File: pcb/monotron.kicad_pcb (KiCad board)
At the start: 2 copper layers, 134.1 x 94 mm, 57 parts, among them J1 Mono / Stereo, J10 DIN5-180, J11 DIN5-180, J12 DE9M, J13 DB25_Female, J14 Mini-DIN-6, J15 Mini-DIN-6, J2 Jack-DC, J3 1x7 Header, J4 AudioJack3, J5 DE9F, J6 1x4 Header, J7 DE15HD, J8 2x6 Header, J9 DIN5-180, U1 TM4C123G_Launchpad, U2 MAX3232, U3 74LS14, U4 6N138, U5 ATmega48A-PU, U6 MCP7940N-xP, Y1 32,768 kHz

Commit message: WIP re-laying out board.
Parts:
- added D2: 1N4148, Diode_THT:D_DO-35_SOD27_P7.62mm_Horizontal, F.Cu at (128.3, 74.9)
- added H1: DP14085, Monotron:DP14085, F.Cu at (67.3, 44.5)
- added J16: Micro_SD_Card_Det, Connector_Card:microSD_HC_Hirose_DM3D-SF, F.Cu at (163.4, 52.3)
- added J17: DNF, Connector_PinHeader_2.54mm:PinHeader_1x07_P2.54mm_Vertical, F.Cu at (176.5, 64.8)
- added R17: 330, Resistor_THT:R_Axial_DIN0204_L3.6mm_D1.6mm_P5.08mm_Horizontal, F.Cu at (239.5, 57.0)
- added R18: 47k, Resistor_THT:R_Axial_DIN0204_L3.6mm_D1.6mm_P5.08mm_Horizontal, F.Cu at (244.5, 50.3)
- added R19: 47k, Resistor_THT:R_Axial_DIN0204_L3.6mm_D1.6mm_P5.08mm_Horizontal, F.Cu at (247.9, 43.6)
- added R20: 47k, Resistor_THT:R_Axial_DIN0204_L3.6mm_D1.6mm_P5.08mm_Horizontal, F.Cu at (240.3, 52.5)
- added R21: 47k, Resistor_THT:R_Axial_DIN0204_L3.6mm_D1.6mm_P5.08mm_Horizontal, F.Cu at (234.5, 61.4)
- C1: value 10u -> 100n; footprint Capacitor_THT:C_Radial_D5.0mm_H5.0mm_P2.00mm -> Capacitor_THT:C_Disc_D5.0mm_W2.5mm_P2.50mm
- C10, C9: value 470n -> 33n
- C11, C12, C13: value 100n -> 470n
- C15, C16: value 12p -> 10u; footprint Capacitor_THT:C_Disc_D4.7mm_W2.5mm_P5.00mm -> Capacitor_THT:C_Radial_D5.0mm_H5.0mm_P2.00mm
- C2: value 10u -> 47u
- C3: value 47u -> 100n; footprint Capacitor_THT:C_Radial_D5.0mm_H5.0mm_P2.00mm -> Capacitor_THT:C_Disc_D5.0mm_W2.5mm_P2.50mm
- C4, C5: value 33n -> 12p
- C8: value 470n -> 100n
- D1: value 1N4148 -> LED; footprint Diode_THT:D_A-405_P12.70mm_Horizontal -> LED_THT:LED_D3.0mm
- J1: value Mono / Stereo -> 2.1mm DC Jack; footprint Connector_PinHeader_2.54mm:PinHeader_1x03_P2.54mm_Vertical -> Connector_BarrelJack:BarrelJack_CUI_PJ-102AH_Horizontal
- J10: value DIN5-180 -> 1x3 Header; footprint Monotron:5P180 DIN Socket -> Connector_PinHeader_2.54mm:PinHeader_1x03_P2.54mm_Vertical
- J11: value DIN5-180 -> DE9M; footprint Monotron:5P180 DIN Socket -> Connector_Dsub:DSUB-9_Male_Horizontal_P2.77x2.84mm_EdgePinOffset7.70mm_Housed_MountingHolesOffset9.12mm
- J12: value DE9M -> Mini-DIN-6; footprint Connector_Dsub:DSUB-9_Male_Horizontal_P2.77x2.84mm_EdgePinOffset7.70mm_Housed_MountingHolesOffset9.12mm -> Monotron:mini-DIN 6
- J13: value DB25_Female -> Mini-DIN-6; footprint Connector_Dsub:DSUB-25_Male_Horizontal_P2.77x2.84mm_EdgePinOffset7.70mm_Housed_MountingHolesOffset9.12mm -> Monotron:mini-DIN 6
- J14: value Mini-DIN-6 -> DB25_Female; footprint Monotron:mini-DIN 6 -> Connector_Dsub:DSUB-25_Male_Horizontal_P2.77x2.84mm_EdgePinOffset7.70mm_Housed_MountingHolesOffset9.12mm
- J15: value Mini-DIN-6 -> DE15HD; footprint Monotron:mini-DIN 6 -> Connector_Dsub:DSUB-15-HD_Female_Horizontal_P2.29x1.98mm_EdgePinOffset8.35mm_Housed_MountingHolesOffset10.89mm
- J2: value Jack-DC -> DE9M; footprint Connector_BarrelJack:BarrelJack_CUI_PJ-102AH_Horizontal -> Connector_Dsub:DSUB-9_Male_Horizontal_P2.77x2.84mm_EdgePinOffset7.70mm_Housed_MountingHolesOffset9.12mm
- J3: value 1x7 Header -> 1x4 Header; footprint Connector_PinHeader_2.54mm:PinHeader_1x07_P2.54mm_Vertical -> Connector_PinHeader_2.54mm:PinHeader_1x04_P2.54mm_Vertical
- J4: value AudioJack3 -> DIN5-180; footprint Connector_Audio:Jack_3.5mm_CUI_SJ1-3533NG_Horizontal -> Monotron:5P180 DIN Socket
- J5: value DE9F -> DIN5-180; footprint Connector_Dsub:DSUB-9_Male_Horizontal_P2.77x2.84mm_EdgePinOffset7.70mm_Housed_MountingHolesOffset9.12mm -> Monotron:5P180 DIN Socket
- J6: value 1x4 Header -> DIN5-180; footprint Connector_PinHeader_2.54mm:PinHeader_1x04_P2.54mm_Vertical -> Monotron:5P180 DIN Socket
- J7: value DE15HD -> 2x6 Header; footprint Connector_Dsub:DSUB-15-HD_Female_Horizontal_P2.29x1.98mm_EdgePinOffset8.35mm_Housed_MountingHolesOffset10.89mm -> Connector_PinHeader_2.54mm:PinHeader_2x06_P2.54mm_Vertical
- J8: value 2x6 Header -> 2x3 Header; footprint Connector_PinHeader_2.54mm:PinHeader_2x06_P2.54mm_Vertical -> Connector_PinHeader_2.54mm:PinHeader_2x03_P2.54mm_Vertical
- J9: value DIN5-180 -> 3.5mm TRS Jack; footprint Monotron:5P180 DIN Socket -> Connector_Audio:Jack_3.5mm_CUI_SJ1-3533NG_Horizontal
- R1: value 150 -> 470; footprint Resistor_THT:R_Axial_DIN0207_L6.3mm_D2.5mm_P2.54mm_Vertical -> Resistor_THT:R_Axial_DIN0204_L3.6mm_D1.6mm_P5.08mm_Horizontal
- R10: footprint Resistor_THT:R_Axial_DIN0411_L9.9mm_D3.6mm_P5.08mm_Vertical -> Resistor_THT:R_Axial_DIN0204_L3.6mm_D1.6mm_P5.08mm_Horizontal
- R11, R12: value 220 -> 270; footprint Resistor_THT:R_Axial_DIN0411_L9.9mm_D3.6mm_P5.08mm_Vertical -> Resistor_THT:R_Axial_DIN0204_L3.6mm_D1.6mm_P5.08mm_Horizontal
- R13, R14: value 220 -> 150; footprint Resistor_THT:R_Axial_DIN0411_L9.9mm_D3.6mm_P5.08mm_Vertical -> Resistor_THT:R_Axial_DIN0204_L3.6mm_D1.6mm_P5.08mm_Horizontal
- R15: value 10K -> 330; footprint Resistor_THT:R_Axial_DIN0411_L9.9mm_D3.6mm_P5.08mm_Vertical -> Resistor_THT:R_Axial_DIN0204_L3.6mm_D1.6mm_P5.08mm_Horizontal
- R16: value 470 -> 330; footprint Resistor_THT:R_Axial_DIN0411_L9.9mm_D3.6mm_P12.70mm_Horizontal -> Resistor_THT:R_Axial_DIN0204_L3.6mm_D1.6mm_P5.08mm_Horizontal
- R2: value 150 -> 10K; footprint Resistor_THT:R_Axial_DIN0207_L6.3mm_D2.5mm_P2.54mm_Vertical -> Resistor_THT:R_Axial_DIN0204_L3.6mm_D1.6mm_P5.08mm_Horizontal
- R3: value 270 -> 470; footprint Resistor_THT:R_Axial_DIN0207_L6.3mm_D2.5mm_P2.54mm_Vertical -> Resistor_THT:R_Axial_DIN0204_L3.6mm_D1.6mm_P5.08mm_Horizontal
- R4: value 270 -> 4.7k; footprint Resistor_THT:R_Axial_DIN0207_L6.3mm_D2.5mm_P2.54mm_Vertical -> Resistor_THT:R_Axial_DIN0204_L3.6mm_D1.6mm_P5.08mm_Horizontal
- R5: footprint Resistor_THT:R_Axial_DIN0411_L9.9mm_D3.6mm_P12.70mm_Horizontal -> Resistor_THT:R_Axial_DIN0204_L3.6mm_D1.6mm_P5.08mm_Horizontal
- R6: value 4.7k -> 220; footprint Resistor_THT:R_Axial_DIN0411_L9.9mm_D3.6mm_P12.70mm_Horizontal -> Resistor_THT:R_Axial_DIN0204_L3.6mm_D1.6mm_P5.08mm_Horizontal
- R7, R8, R9: value 330 -> 220; footprint Resistor_THT:R_Axial_DIN0411_L9.9mm_D3.6mm_P12.70mm_Horizontal -> Resistor_THT:R_Axial_DIN0204_L3.6mm_D1.6mm_P5.08mm_Horizontal
- U1: value TM4C123G_Launchpad -> 74LS14; footprint Launchpad:Launchpad_4x10 -> Package_DIP:DIP-14_W7.62mm
- U2: value MAX3232 -> 6N138; footprint Package_DIP:DIP-16_W7.62mm -> Package_DIP:DIP-8_W7.62mm
- U3: value 74LS14 -> MCP7940N-xP; footprint Package_DIP:DIP-14_W7.62mm -> Package_DIP:DIP-8_W7.62mm
- U4: value 6N138 -> TM4C123G_Launchpad; footprint Package_DIP:DIP-8_W7.62mm -> Monotron:Launchpad_4x10
- U6: value MCP7940N-xP -> MAX3232; footprint Package_DIP:DIP-8_W7.62mm -> Package_DIP:DIP-16_W7.62mm
- moved C3 159.9 mm to (229.5, 109.4), turned to 90 degrees
- moved J12 133.2 mm to (67.7, 80.0), turned to 90 degrees
- moved R16 128.6 mm to (243.7, 34.4)
- moved R6 126.9 mm to (237.9, 36.6)
- moved J11 121.8 mm to (77.8, 98.7), turned to 270 degrees
- moved J3 118.1 mm to (194.3, 82.5)
- moved R8 117.9 mm to (216.9, 45.5)
- moved R7 117.7 mm to (212.4, 51.4)
- moved R9 115.3 mm to (218.6, 43.3)
- moved J2 99.9 mm to (151.1, 120.7), turned to 0 degrees
- moved J13 98.1 mm to (67.7, 61.4), turned to 90 degrees
- moved C11 90.3 mm to (92.8, 102.9), turned to 0 degrees
- moved BT1 84.3 mm to (110.5, 77.5), turned to 180 degrees
- moved C17 82.2 mm to (238.7, 124.7)
- moved C14 79.6 mm to (231.1, 71.3), turned to 270 degrees
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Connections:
- net /DSR renamed Net-(J12-Pad6)
- C1 pad 1: Net-(C1-Pad1) -> +5V
- C1 pad 2: Net-(C1-Pad2) -> GND
- C10 pad 1: GND -> Net-(C10-Pad1)
- C10 pad 2: Net-(C10-Pad2) -> GND
- C11 pad 1: +5V -> Net-(C11-Pad1)
- C11 pad 2: GND -> Net-(C11-Pad2)
- C12 pad 1: +5V -> Net-(C12-Pad1)
- C12 pad 2: GND -> Net-(C12-Pad2)
- C13 pad 1: +5V -> GND
- C13 pad 2: GND -> Net-(C13-Pad2)
- C15 pad 1: GND -> Net-(C15-Pad1)
- C16 pad 1: GND -> Net-(C10-Pad1)
- C17 pad 1: +3V3 -> Net-(C12-Pad1)
- C2 pad 1: Net-(C2-Pad1) -> +5V
- C2 pad 2: Net-(C2-Pad2) -> GND
- C3 pad 1: +5V -> +3V3
- C4 pad 1: Net-(C1-Pad1) -> GND
- C4 pad 2: GND -> Net-(C4-Pad2)
- C5 pad 1: Net-(C2-Pad1) -> GND
- C5 pad 2: GND -> Net-(C5-Pad2)
- C7 pad 1: Net-(C7-Pad1) -> +5V
- C8 pad 1: Net-(C8-Pad1) -> +5V
- C8 pad 2: Net-(C8-Pad2) -> GND
- C9 pad 1: Net-(C7-Pad1) -> Net-(C15-Pad1)
- C9 pad 2: Net-(C9-Pad2) -> GND
- D1 pad 1: Net-(D1-Pad1) -> /PD2_SD_ACT
- J1 pad 1: Net-(C1-Pad2) -> +5V
- J1 pad 2: Net-(J1-Pad2) -> GND
- J1 pad 3: Net-(C2-Pad2) -> (no net)
- J10 pad 1: Net-(J10-Pad1) -> Net-(C15-Pad2)
- J10 pad 2: GND -> Net-(J10-Pad2)
- J10 pad 3: Net-(J10-Pad3) -> Net-(C16-Pad2)
- J11 pad 2: Net-(J11-Pad2) -> /RS232_RX
- J11 pad 3: Net-(J11-Pad3) -> /RS232_TX
- J11 pad 5: Net-(D1-Pad2) -> GND
- J11 pad 6: (no net) -> Net-(J11-Pad6)
- J11 pad 7: (no net) -> /RS232_RTS
- J12 pad 1: /DCD -> /KB_DATA
- J12 pad 2: /RS232_RX -> Net-(J12-Pad2)
- J12 pad 3: /RS232_TX -> GND
- J12 pad 4: /DTR -> +5V
- J12 pad 5: GND -> /KB_CLK
- J12 pad 7: /RS232_RTS -> (no net)
- J12 pad 8: /RS232_CTS -> (no net)
- J12 pad 9: /RI -> (no net)
- J13 pad 1: /Monotron I/O Expansion/STROBE -> /MS_DATA
- J13 pad 2: /Monotron I/O Expansion/D0 -> Net-(J13-Pad2)
- J13 pad 3: /Monotron I/O Expansion/D1 -> GND
- J13 pad 4: /Monotron I/O Expansion/D2 -> +5V
- J13 pad 5: /Monotron I/O Expansion/D3 -> /MS_CLK
- J13 pad 6: /Monotron I/O Expansion/D4 -> Net-(J13-Pad6)
- J13 pad 7: /Monotron I/O Expansion/D5 -> (no net)
- J13 pad 8: /Monotron I/O Expansion/D6 -> (no net)
- J13 pad 9: /Monotron I/O Expansion/D7 -> (no net)
- J14 pad 1: /Monotron I/O Expansion/KB_DATA -> /STROBE
- J14 pad 2: Net-(J14-Pad2) -> /D0
- J14 pad 3: GND -> /D1
- J14 pad 4: +5V -> /D2
- J14 pad 5: /Monotron I/O Expansion/KB_CLK -> /D3_MOSI
- J14 pad 6: Net-(J14-Pad6) -> /D4_MISO
- J14 pad 7: (no net) -> /D5_SCK
- J14 pad 8: (no net) -> /D6
- J14 pad 9: (no net) -> /D7
- J15 pad 1: /Monotron I/O Expansion/MS_DATA -> Net-(J15-Pad1)
- J15 pad 3: GND -> Net-(J15-Pad3)
- J15 pad 4: +5V -> Net-(J15-Pad4)
- J15 pad 5: /Monotron I/O Expansion/MS_CLK -> GND
- J15 pad 6: Net-(J15-Pad6) -> GND
- J15 pad 7: (no net) -> GND
- J15 pad 8: (no net) -> GND
- J15 pad 9: (no net) -> Net-(J15-Pad9)
- J2 pad 1: +5V -> /PE2_JS_UP
- J2 pad 2: GND -> /PE3_JS_DOWN
- J2 pad 3: (no net) -> /PD6_JS_LEFT
- J3 pad 1: Net-(J3-Pad1) -> GND
- J3 pad 2: /PA4_SD_MISO -> +5V
- J3 pad 3: GND -> /PA7_I2C_SDA
- J3 pad 4: /PA2_SD_CLK -> /PA6_I2C_SCL
- J5 pad 1: /PE2_JS_UP -> Net-(J5-Pad1)
- J5 pad 2: /PE3_JS_DOWN -> Net-(J5-Pad2)
- J5 pad 3: /PD6_JS_LEFT -> Net-(J5-Pad3)
- J5 pad 4: /PD7_JS_RIGHT -> Net-(J5-Pad4)
- J5 pad 5: Net-(J5-Pad5) -> Net-(D2-Pad1)
- J5 pad 6: /PF4_JS_FIRE -> (no net)
- J5 pad 7: Net-(J5-Pad7) -> (no net)
- J6 pad 1: GND -> Net-(J6-Pad1)
- J6 pad 2: +5V -> GND
- J6 pad 3: /PA7_I2C_SDA -> Net-(J6-Pad3)
- J6 pad 4: /PA6_I2C_SCL -> Net-(J6-Pad4)
- J7 pad 1: Net-(J7-Pad1) -> GND
- J7 pad 10: Net-(J7-Pad10) -> /PB0_U1RX
- J7 pad 11: Net-(J7-Pad11) -> Net-(C12-Pad1)
- J7 pad 12: Net-(J7-Pad12) -> +3V3
- J7 pad 2: Net-(J7-Pad2) -> GND
- J7 pad 4: Net-(J7-Pad4) -> /PC5_U1CTS
- J7 pad 5: GND -> Net-(J7-Pad5)
- J7 pad 6: GND -> /PC4_U1RTS
- J7 pad 7: GND -> Net-(J7-Pad7)
- J7 pad 8: GND -> /PB1_U1TX
- J8 pad 1: GND -> /D4_MISO
- J8 pad 2: GND -> +5V
- J8 pad 3: /DTE_CTS -> /D5_SCK
- J8 pad 4: /PC5_U1CTS -> /D3_MOSI
- J8 pad 5: /DTE_RTS -> Net-(J8-Pad5)
- J8 pad 6: /PC4_U1RTS -> GND
- R1 pad 1: Net-(C1-Pad1) -> +3V3
- R1 pad 2: GND -> /PC6_MIDI_IN
- R10 pad 2: Net-(J9-Pad4) -> Net-(J6-Pad4)
- R11 pad 1: +5V -> /PE4_AUDIO_L
- R11 pad 2: Net-(J10-Pad4) -> Net-(C15-Pad1)
- R12 pad 1: Net-(R12-Pad1) -> /PE5_AUDIO_R
- R12 pad 2: Net-(J10-Pad5) -> Net-(C10-Pad1)
- R13 pad 1: Net-(J9-Pad5) -> Net-(C15-Pad1)
- R13 pad 2: Net-(R13-Pad2) -> GND
- R14 pad 1: Net-(D1-Pad1) -> Net-(C10-Pad1)
- R14 pad 2: Net-(J11-Pad4) -> GND
- R15 pad 1: Net-(R15-Pad1) -> Net-(J15-Pad1)
- R15 pad 2: GND -> /PF1_VGA_RED
- R16 pad 1: +3V3 -> Net-(J15-Pad2)
- R16 pad 2: /PC6_MIDI_IN -> /PB7_VGA_GRN
- R2 pad 1: Net-(C2-Pad1) -> Net-(R2-Pad1)
- R3 pad 1: /PE4_AUDIO_L -> Net-(D1-Pad2)
- R3 pad 2: Net-(C1-Pad1) -> +3V3
- R4 pad 1: /PE5_AUDIO_R -> /PA6_I2C_SCL
- R4 pad 2: Net-(C2-Pad1) -> +5V
- R5 pad 1: /PA6_I2C_SCL -> +5V
- R5 pad 2: +5V -> /PA7_I2C_SDA
- R6 pad 1: +5V -> Net-(R6-Pad1)
- R6 pad 2: /PA7_I2C_SDA -> Net-(J4-Pad5)
- R7 pad 1: Net-(J7-Pad1) -> Net-(R7-Pad1)
- R7 pad 2: /PF1_VGA_RED -> Net-(J6-Pad5)
- R8 pad 1: Net-(J7-Pad2) -> Net-(D2-Pad2)
- R8 pad 2: /PB7_VGA_GRN -> Net-(J5-Pad4)
- R9 pad 1: Net-(J7-Pad3) -> +5V
- R9 pad 2: /PD3_VGA_BLU -> Net-(J4-Pad4)
- U2 pad 1: Net-(C6-Pad1) -> Net-(U2-Pad1)
- U2 pad 2: Net-(C9-Pad2) -> Net-(D2-Pad1)
- U2 pad 3: Net-(C6-Pad2) -> Net-(D2-Pad2)
- U2 pad 4: Net-(C8-Pad1) -> Net-(U2-Pad4)
- U2 pad 5: Net-(C8-Pad2) -> GND
- U2 pad 6: Net-(C10-Pad2) -> /PC6_MIDI_IN
- U2 pad 7: /RS232_RTS -> Net-(R2-Pad1)
- U2 pad 8: /RS232_CTS -> +5V
- U3 pad 1: /PC6_MIDI_IN -> Net-(C4-Pad2)
- U3 pad 2: Net-(U3-Pad2) -> Net-(C5-Pad2)
- U3 pad 3: Net-(U3-Pad3) -> +BATT
- U3 pad 4: Net-(R13-Pad2) -> GND
- U3 pad 5: Net-(U3-Pad2) -> /PA7_I2C_SDA
- U3 pad 6: Net-(R12-Pad1) -> /PA7_I2C_SDA
- U3 pad 7: GND -> Net-(U3-Pad7)
- U3 pad 8: Net-(U3-Pad3) -> +3V3
- U5 pad 1: /Monotron I/O Expansion/SELPRIN -> Net-(J8-Pad5)
- U5 pad 10: /Monotron I/O Expansion/D7 -> /D7
- U5 pad 11: /Monotron I/O Expansion/ERROR -> /ERROR
- U5 pad 12: /Monotron I/O Expansion/AUTOF -> /AUTOF
- U5 pad 13: /Monotron I/O Expansion/STROBE -> /STROBE
- U5 pad 14: /Monotron I/O Expansion/D0 -> /D0
- U5 pad 15: /Monotron I/O Expansion/D1 -> /D1
- U5 pad 16: /Monotron I/O Expansion/D2 -> /D2
- U5 pad 17: /Monotron I/O Expansion/D3 -> /D3_MOSI
- U5 pad 18: /Monotron I/O Expansion/D4 -> /D4_MISO
- U5 pad 19: /Monotron I/O Expansion/D5 -> /D5_SCK
- U5 pad 2: /PE1_U7TX -> /PE0_U7RX
- U5 pad 23: /Monotron I/O Expansion/KB_CLK -> /KB_CLK
- U5 pad 24: /Monotron I/O Expansion/MS_CLK -> /MS_CLK
- U5 pad 25: /Monotron I/O Expansion/KB_DATA -> /KB_DATA
- U5 pad 26: /Monotron I/O Expansion/MS_DATA -> /MS_DATA
- U5 pad 27: /Monotron I/O Expansion/INIT -> /SELPRIN
- U5 pad 28: /Monotron I/O Expansion/SEL -> /SEL
- U5 pad 3: /PE0_U7RX -> /PE1_U7TX
- U5 pad 4: /Monotron I/O Expansion/ACK -> /ACK
- U5 pad 5: /Monotron I/O Expansion/BUSY -> /BUSY
- U5 pad 6: /Monotron I/O Expansion/PE -> /PE
- U5 pad 9: /Monotron I/O Expansion/D6 -> /D6
- U6 pad 1: Net-(C15-Pad2) -> Net-(C6-Pad1)
- U6 pad 2: Net-(C16-Pad2) -> Net-(C12-Pad2)
- U6 pad 3: +BATT -> Net-(C6-Pad2)
- U6 pad 4: GND -> Net-(C11-Pad1)
- U6 pad 5: /PA7_I2C_SDA -> Net-(C11-Pad2)
- U6 pad 6: /PA6_I2C_SCL -> Net-(C13-Pad2)
- U6 pad 7: Net-(U6-Pad7) -> /RS232_RTS
- U6 pad 8: +3V3 -> /RS232_CTS
- Y1 pad 1: Net-(C15-Pad2) -> Net-(C4-Pad2)
- Y1 pad 2: Net-(C16-Pad2) -> Net-(C5-Pad2)
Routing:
- net GND: track 589.7 -> 0.00 mm
- net +5V: track 299.7 -> 0.00 mm, vias 1 -> 0
- net +3V3: track 156.0 -> 0.00 mm, vias 1 -> 0
- net /PE4_AUDIO_L: track 126.3 -> 0.00 mm, vias 1 -> 0
- net /PC6_MIDI_IN: track 109.1 -> 0.00 mm, vias 1 -> 0
- net /PE5_AUDIO_R: track 101.5 -> 0.00 mm, vias 1 -> 0
- net /PC7_MIDI_OUT: track 96.2 -> 0.00 mm, vias 2 -> 0
- net Net-(D1-Pad2): track 92.4 -> 0.00 mm
- net /Monotron I/O Expansion/KB_DATA: track 90.0 -> 0.00 mm, vias 1 -> 0
- net /Monotron I/O Expansion/KB_CLK: track 90.0 -> 0.00 mm
- net /PF4_JS_FIRE: track 89.6 -> 0.00 mm
- net /PB4_VGA_HSYNC: track 80.9 -> 0.00 mm, vias 2 -> 0
- net /PD6_JS_LEFT: track 79.3 -> 0.00 mm
- net /PD7_JS_RIGHT: track 78.5 -> 0.00 mm
- net /Monotron I/O Expansion/MS_DATA: track 77.4 -> 0.00 mm, vias 2 -> 0
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- removed copper zone on B.Cu, net GND
- removed copper zone on F.Cu, net GND
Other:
- board size 134.1 x 94 mm -> 140 x 85 mm
- board text removed: "3v3"
- board text removed: "GND"
- board text removed: "MIDI In"
- board text removed: "MIDI Thru"
- board text removed: "RX"
- board text removed: "TX"

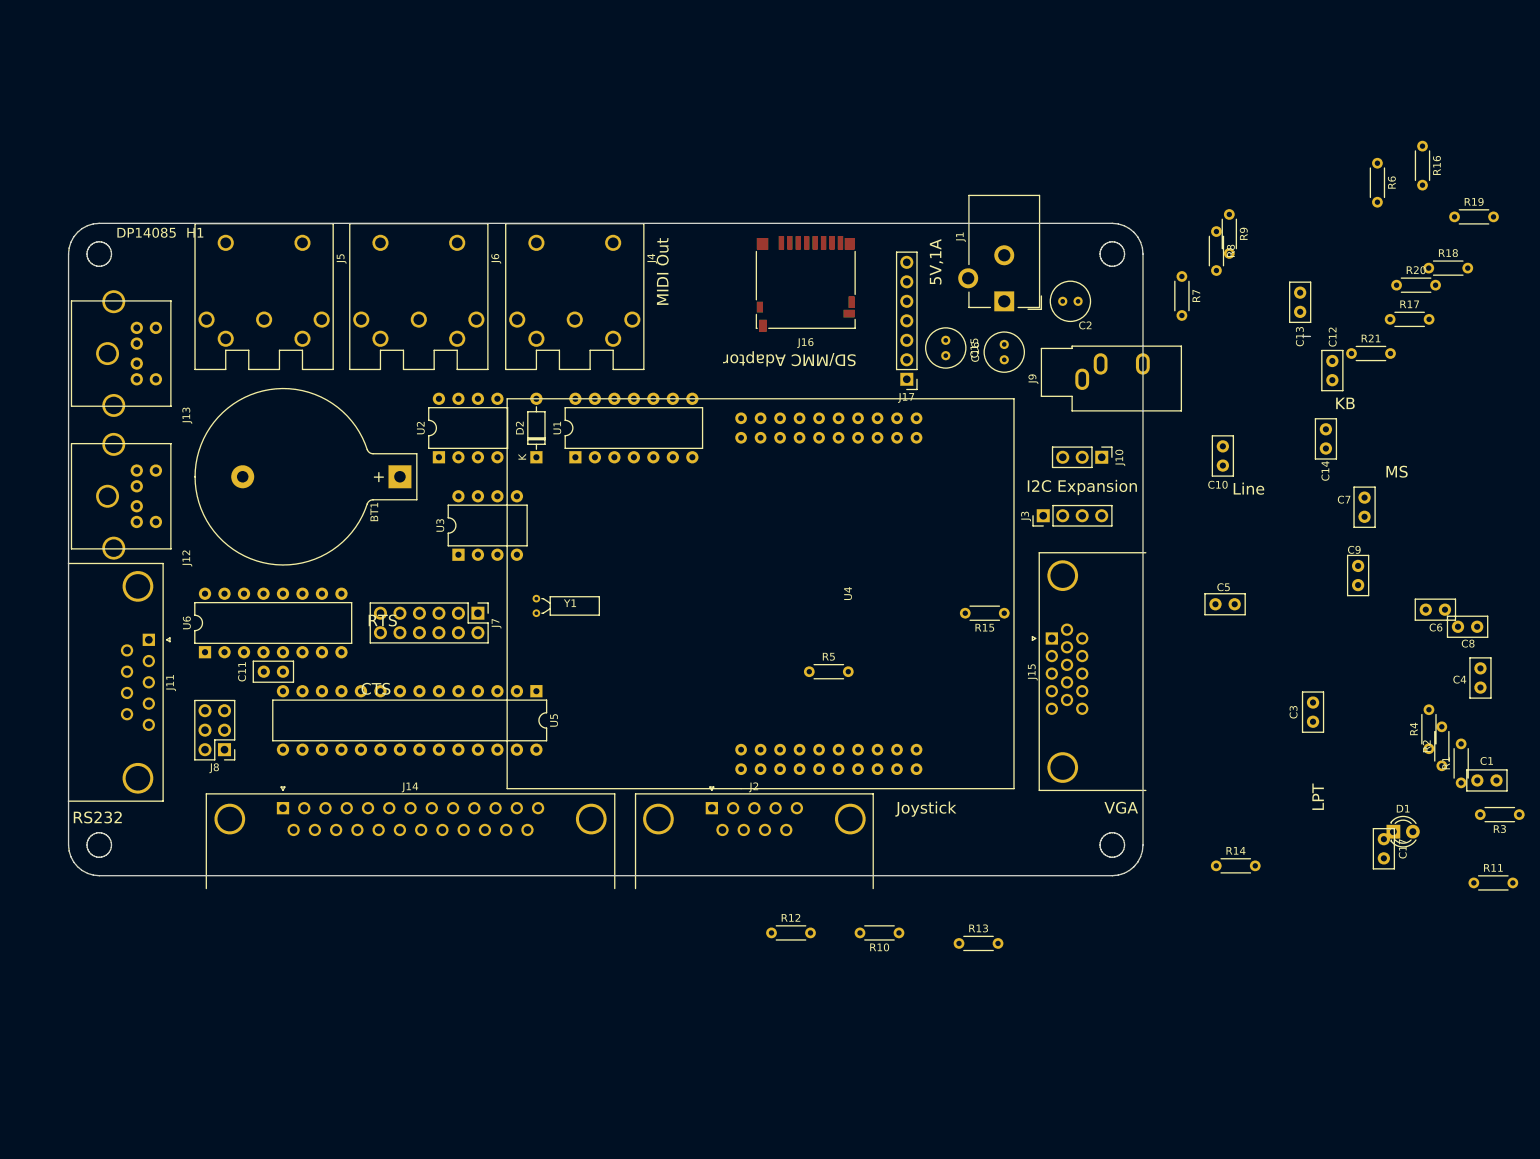
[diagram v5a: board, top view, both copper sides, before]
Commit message: Working on schematic. Deleted power jack in favour of Launchpad USB. Added MCP23017 for twin joystick support.
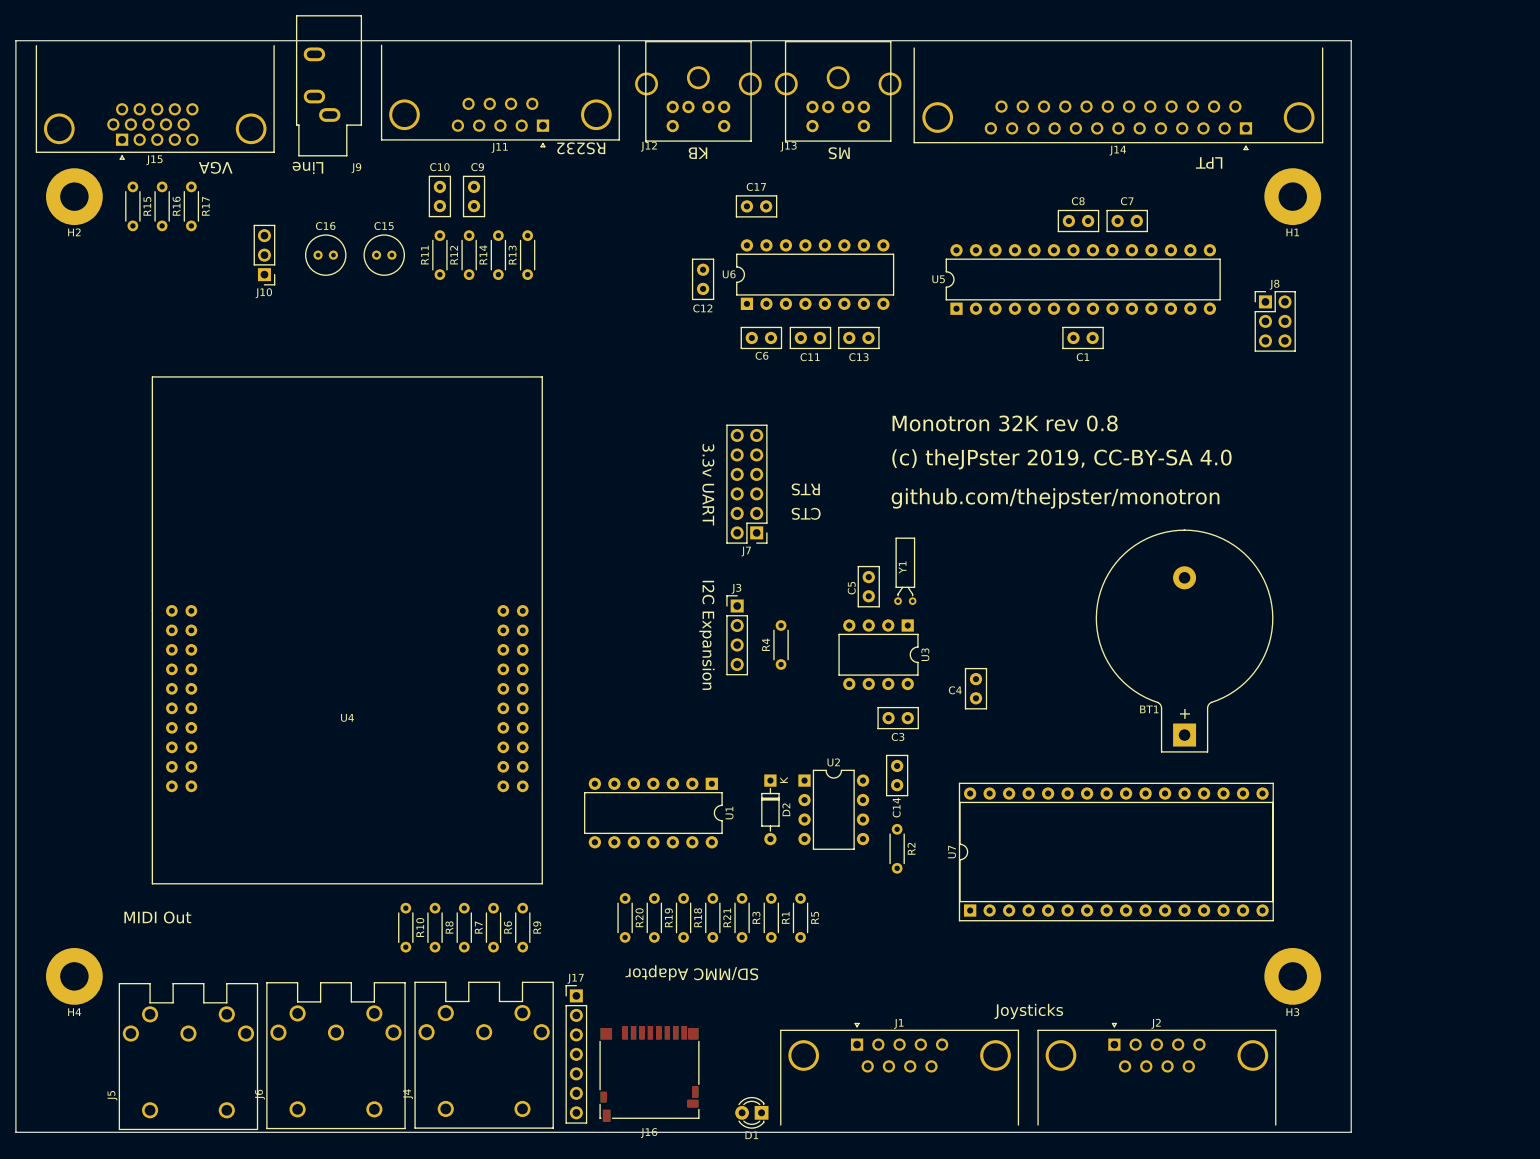
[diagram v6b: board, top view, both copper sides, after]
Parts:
- removed C2: 47u, Capacitor_THT:C_Radial_D5.0mm_H5.0mm_P2.00mm
- added H2: 3.7mm, MountingHole:MountingHole_3.7mm_Pad, F.Cu at (68.1, 41.0)
- added H3: 3.7mm, MountingHole:MountingHole_3.7mm_Pad, F.Cu at (226.8, 142.6)
- added H4: 3.7mm, MountingHole:MountingHole_3.7mm_Pad, F.Cu at (68.1, 142.6)
- added U7: MCP23017, Package_DIP:DIP-32_W15.24mm_Socket, F.Cu at (184.8, 134.0)
- H1: value DP14085 -> 3.7mm; footprint Monotron:DP14085 -> MountingHole:MountingHole_3.7mm_Pad
- J1: value 2.1mm DC Jack -> DE9M; footprint Connector_BarrelJack:BarrelJack_CUI_PJ-102AH_Horizontal -> Connector_Dsub:DSUB-9_Male_Horizontal_P2.77x2.84mm_EdgePinOffset7.70mm_Housed_MountingHolesOffset9.12mm
- moved R16 164.3 mm to (79.5, 39.7)
- moved H1 159.5 mm to (226.8, 41.0), turned to 180 degrees
- moved R17 157.1 mm to (83.3, 39.7), turned to 270 degrees
- moved R11 156.3 mm to (115.7, 51.1), turned to 90 degrees
- moved J14 153.6 mm to (220.7, 32.1), turned to 180 degrees
- moved R6 150.6 mm to (122.7, 133.7)
- moved J8 147.7 mm to (223.3, 54.7), turned to 0 degrees
- moved J15 137.5 mm to (74.3, 33.6), turned to 180 degrees
- moved R19 137.0 mm to (143.6, 132.4), turned to 270 degrees
- moved R8 134.7 mm to (115.1, 133.7)
- moved R9 129.0 mm to (126.5, 133.7)
- moved R20 128.4 mm to (139.8, 132.4), turned to 270 degrees
- moved R18 127.2 mm to (147.4, 132.4), turned to 270 degrees
- moved R15 126.4 mm to (75.7, 39.7), turned to 270 degrees
- moved R7 124.6 mm to (118.9, 133.7)
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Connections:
- net /ACK renamed /LPT_ACK
- net /AUTOF renamed /LPT_AUTOF
- net /BUSY renamed /LPT_BUSY
- net /D0 renamed /LPT_D0
- net /D1 renamed /LPT_D1
- net /D2 renamed /LPT_D2
- net /D3_MOSI renamed /LPT_D3_MOSI
- net /D4_MISO renamed /LPT_D4_MISO
- net /D5_SCK renamed /LPT_D5_SCK
- net /D6 renamed /LPT_D6
- net /D7 renamed /LPT_D7
- net /ERROR renamed /LPT_ERROR
- net /INIT renamed /LPT_INIT
- net /PB3_SPARE renamed /PB3_NC
- net /PB6_SPARE renamed /PD1_PB6_NC
- net /PE renamed /LPT_PE
- net /SEL renamed /LPT_SEL
- net /SELPRIN renamed /LPT_SELPRIN
- net /STROBE renamed /LPT_STROBE
- J1 pad 1: +5V -> Net-(J1-Pad1)
- J1 pad 2: GND -> Net-(J1-Pad2)
- J1 pad 3: (no net) -> Net-(J1-Pad3)
- J5 pad 4: Net-(J5-Pad4) -> Net-(D2-Pad1)
- J5 pad 5: Net-(D2-Pad1) -> Net-(J5-Pad5)
- R8 pad 2: Net-(J5-Pad4) -> Net-(J5-Pad5)
- U5 pad 2: /PE0_U7RX -> /PE1_U7TX
- U5 pad 3: /PE1_U7TX -> /PE0_U7RX
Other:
- board size 140 x 85 mm -> 174 x 142.2 mm
- board text added: "(c) theJPster 2019, CC-BY-SA 4.0"
- board text added: "3.3v UART"
- board text added: "Joysticks"
- board text added: "Monotron 32K rev 0.8"
- board text added: "github.com/thejpster/monotron"
- board text removed: "5V,1A"
- board text removed: "Joystick"
